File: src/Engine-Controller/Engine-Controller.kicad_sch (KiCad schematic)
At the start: 21 parts, among them J1 Jumper_NO, J2 Jumper_NO, P3 3220-20-0200-00, U1 STM32H750VBTx, Y1 ECS-240-18-33-JGN-TR

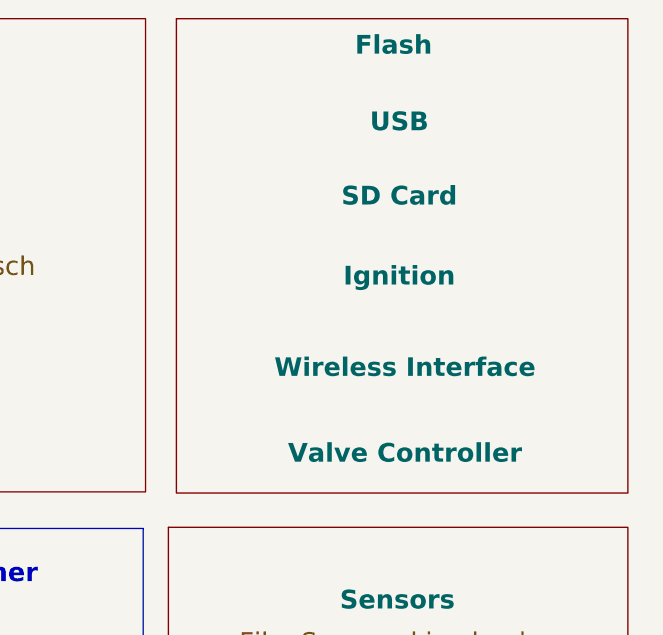
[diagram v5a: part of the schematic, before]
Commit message: removed wireless interface connector
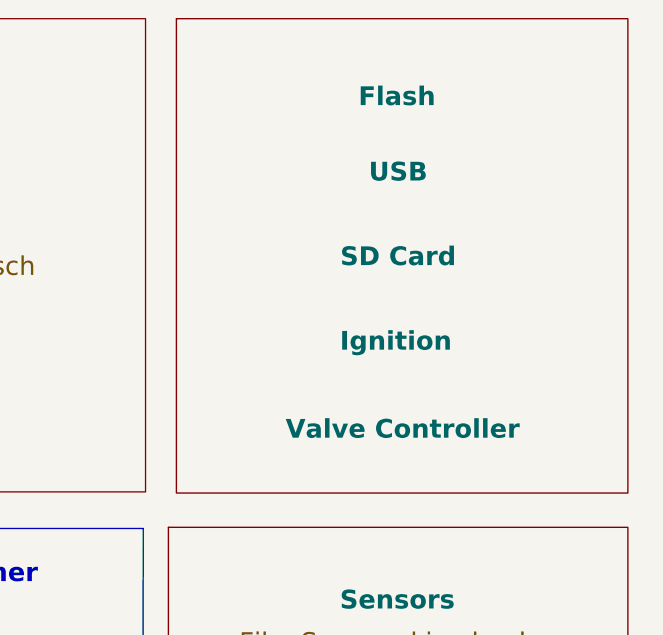
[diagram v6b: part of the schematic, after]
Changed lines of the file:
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@@
       (effects (font (size 1.27 1.27)) (justify left top) hide)
     )
-    (property "Field2" "Ignition" (at 256.54 48.895 0)
+    (property "Field2" "Ignition" (at 256.159 56.134 0)
       (effects (font (size 2.08 2.08) bold))
     )
-    (property "Field3" "USB" (at 256.54 31.75 0)
+    (property "Field3" "USB" (at 256.413 37.338 0)
       (effects (font (size 2.08 2.08) bold))
     )
-    (property "Field4" "Flash" (at 255.905 23.241 0)
+    (property "Field4" "Flash" (at 256.286 28.956 0)
       (effects (font (size 2.08 2.08) bold))
     )
-    (property "Field5" "SD Card" (at 256.54 40.005 0)
+    (property "Field5" "SD Card" (at 256.413 46.736 0)
       (effects (font (size 2.08 2.08) bold))
     )
-    (property "Field6" "Valve Controller" (at 257.175 68.58 0)
+    (property "Field6" "Valve Controller" (at 256.921 65.913 0)
       (effects (font (size 2.08 2.08) bold))
     )
-    (property "Field7" "Wireless Interface" (at 257.175 59.055 0)
-      (effects (font (size 2.0574 2.0574) bold))
-    )
     (instances
